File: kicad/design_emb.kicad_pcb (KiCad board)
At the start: 2 copper layers, 79.9 x 98.8 mm, 116 parts, among them J1 Conn_01x04, J2 Barrel_Jack, J3 USB_A, J4 Conn_01x03, J5 Conn_02x11_Counter_Clockwise, J6 Conn_02x10_Counter_Clockwise, J7 Screw_Terminal_01x02, J8 Screw_Terminal_01x02, K1 SANYOU_SRD_Form_C, K2 SANYOU_SRD_Form_C, Q1 MMBT3904, Q2 MMBT3904, SW1 SW_Push, SW3 SW_Push, U1 SRX.X.TCT, U10 S25FL116KOXNFIQ-11, U2 SRX.X.TCT, U3 STM32F446ZETx, U4 ICE40HX1K, U5 TLV1117LV33DCYR, U6 TLV1117LV33DCYR, U7 TLV1117LV12DCYR, U8 OMEGA2, U9 RCLAMP0502B

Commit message: ruteo
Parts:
- moved J3 0.85 mm to (148.8, 94.4)
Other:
- board size 79.9 x 98.8 mm -> 79.8 x 98.9 mm
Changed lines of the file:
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@@
   )
   (module Connectors:USB_A (layer F.Cu)
-    (at 148.844 95.25 180)
+    (at 148.8059 94.3991 180)
     (descr "USB A connector")
     (tags "USB USB_A")
@@
     )
   )
-  (gr_line (start 159.0802 83.0326) (end 79.1718 82.9564) (layer Edge.Cuts) (width 0.15))
-  (gr_line (start 158.9786 181.6989) (end 159.004 83.058) (layer Edge.Cuts) (width 0.15))
-  (gr_line (start 79.2353 181.7878) (end 79.1845 82.9818) (layer Edge.Cuts) (width 0.2))
+  (gr_line (start 158.9913 83.0326) (end 79.1718 82.9564) (layer Edge.Cuts) (width 0.15))
+  (gr_line (start 158.9913 181.7243) (end 159.004 83.058) (layer Edge.Cuts) (width 0.15))
+  (gr_line (start 79.2226 181.7878) (end 79.1718 82.9818) (layer Edge.Cuts) (width 0.2))
   (dimension 99.174366 (width 0.3) (layer F.SilkS)
-    (gr_text "99,174 mm" (at 73.454835 132.075698 89.93396571) (layer F.SilkS)
+    (gr_text "99,174 mm" (at 72.286058 132.546979 89.93396571) (layer F.SilkS)
       (effects (font (size 1.5 1.5) (thickness 0.3)))
     )
-    (feature1 (pts (xy 75.910241 82.491312) (xy 75.025564 82.490292)))
-    (feature2 (pts (xy 75.795941 181.665612) (xy 74.911264 181.664592)))
-    (crossbar (pts (xy 75.497684 181.665268) (xy 75.611984 82.490968)))
-    (arrow1a (pts (xy 75.611984 82.490968) (xy 76.197106 83.618147)))
-    (arrow1b (pts (xy 75.611984 82.490968) (xy 75.024265 83.616795)))
-    (arrow2a (pts (xy 75.497684 181.665268) (xy 76.085403 180.539441)))
-    (arrow2b (pts (xy 75.497684 181.665268) (xy 74.912562 180.538089)))
-  )
-  (gr_line (start 158.9532 181.7243) (end 79.2988 181.8005) (layer Edge.Cuts) (width 0.15))
+    (feature1 (pts (xy 74.741464 82.962593) (xy 73.856787 82.961573)))
+    (feature2 (pts (xy 74.627164 182.136893) (xy 73.742487 182.135873)))
+    (crossbar (pts (xy 74.328907 182.136549) (xy 74.443207 82.962249)))
+    (arrow1a (pts (xy 74.443207 82.962249) (xy 75.028329 84.089428)))
+    (arrow1b (pts (xy 74.443207 82.962249) (xy 73.855488 84.088076)))
+    (arrow2a (pts (xy 74.328907 182.136549) (xy 74.916626 181.010722)))
+    (arrow2b (pts (xy 74.328907 182.136549) (xy 73.743785 181.00937)))
+  )
+  (gr_line (start 158.9913 181.7243) (end 79.2099 181.8132) (layer Edge.Cuts) (width 0.15))
   (dimension 80.086204 (width 0.3) (layer F.SilkS)
     (gr_text "80,086 mm" (at 119.154383 183.078787 0.01817182924) (layer F.SilkS)

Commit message: design_emb.kicad_pcb
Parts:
- C1, D10, R15: moved to B.Cu
- moved Q2 65.6 mm to (94.2, 130.8), turned to 90 degrees
- moved C39 64.0 mm to (120.0, 118.2)
- moved C41 64.0 mm to (120.0, 115.6)
- moved C44 64.0 mm to (120.0, 120.7)
- moved C52 64.0 mm to (120.0, 113.0)
- moved R13 63.0 mm to (90.2, 129.5), turned to 270 degrees
- moved D8 59.9 mm to (94.0, 134.6)
- moved C42 56.0 mm to (125.1, 113.0)
- moved C45 56.0 mm to (125.1, 115.6)
- moved D7 55.0 mm to (99.1, 132.1)
- moved R12 52.4 mm to (99.1, 129.5)
- moved C26 50.9 mm to (125.1, 118.1)
- moved Q1 50.3 mm to (90.2, 125.7), turned to 180 degrees
- moved C43 34.4 mm to (131.4, 88.9)
- moved C40 34.4 mm to (131.4, 91.4)
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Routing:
- net VDD: track 57.8 -> 201.1 mm, vias 2 -> 7
- net Net-(D11-Pad2): track 0.00 -> 75.2 mm, vias 0 -> 2
- net +5VA: track 16.0 -> 82.7 mm, vias 3 -> 4
- net Net-(D12-Pad2): track 0.00 -> 63.2 mm, vias 0 -> 1
- net /SERIAL_TX: track 0.00 -> 58.3 mm, vias 0 -> 1
- net /SERIAL_RX: track 0.00 -> 51.4 mm, vias 0 -> 1
- net GND: track 0.00 -> 40.6 mm, vias 0 -> 1
- net /3V3_O: track 0.00 -> 29.9 mm
- net Net-(J7-Pad2): track 0.00 -> 27.3 mm
- net /Sheet2/RESET: track 0.00 -> 24.7 mm, vias 0 -> 1
- net Net-(J8-Pad1): track 0.00 -> 23.6 mm
- net /Sheet2/USB-: track 0.00 -> 21.4 mm, vias 0 -> 1
- net /Sheet2/SPI1: track 64.4 -> 82.5 mm, vias 1 -> 5
- net /Sheet2/USB+: track 0.00 -> 17.6 mm, vias 0 -> 1
- net Net-(J3-Pad5): track 0.00 -> 16.6 mm
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
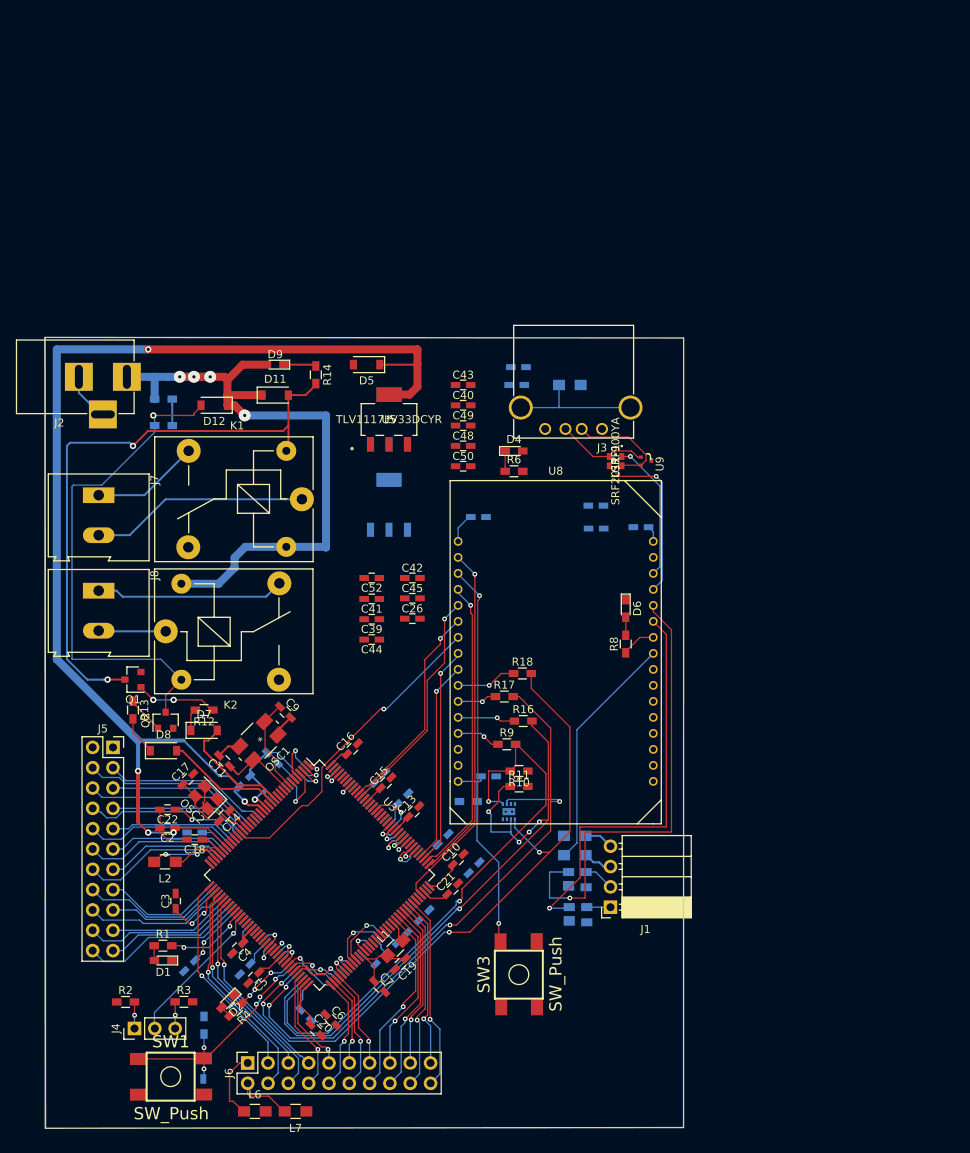
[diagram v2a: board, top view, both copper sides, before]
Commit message: plano de tierra y modificación de señales
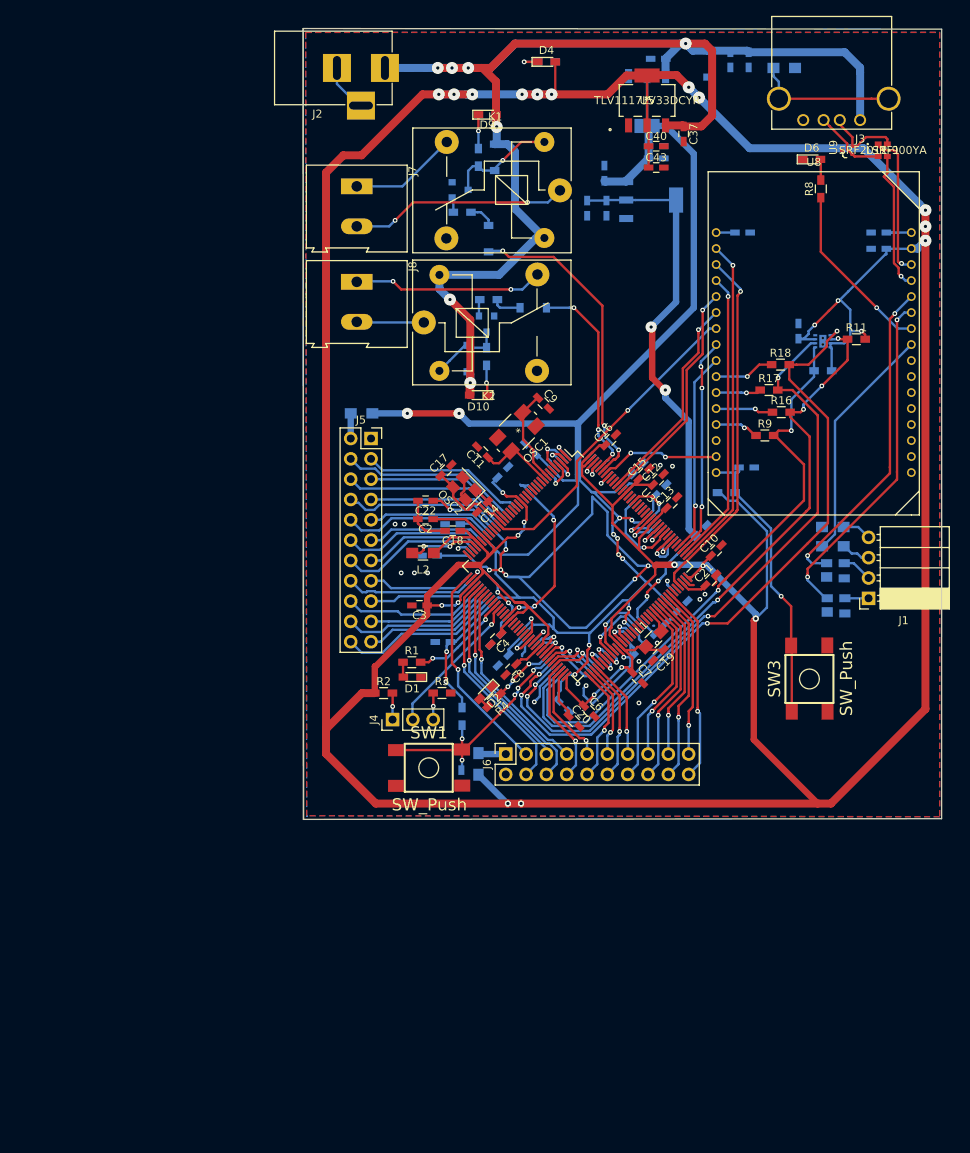
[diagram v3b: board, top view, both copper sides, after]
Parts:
- removed C35, C5: 100nF, Capacitors_SMD:C_0603_HandSoldering
- C12, C37, C8, D10: moved to F.Cu
- C26, C39, C41, C42, C44, C45, C48, C49, C50, C52, D11, D12, D5, D7, D8, L6, L7, Q1, Q2, R10, R12, R13, R14, R6: moved to B.Cu
- moved L7 87.6 mm to (118.7, 92.5), turned to 0 degrees
- moved Q1 73.6 mm to (131.1, 64.5), turned to 0 degrees
- moved D8 72.1 mm to (140.2, 79.2)
- moved D7 71.0 mm to (134.6, 70.6), turned to 270 degrees
- moved U10 70.7 mm to (176.4, 83.4), turned to 90 degrees
- moved R12 70.1 mm to (131.3, 67.3), turned to 0 degrees
- moved R11 70.0 mm to (180.6, 83.2)
- moved C44 69.9 mm to (155.6, 60.6), turned to 0 degrees
- moved R13 67.9 mm to (134.6, 78.2), turned to 0 degrees
- moved C41 66.8 mm to (155.6, 59.1), turned to 0 degrees
- moved Q2 63.7 mm to (134.4, 81.3), turned to 270 degrees
- moved C39 62.9 mm to (149.1, 62.4), turned to 90 degrees
- moved R10 62.8 mm to (176.4, 87.1)
- moved C50 62.1 mm to (167.1, 48.3), turned to 270 degrees
- moved R8 61.9 mm to (176.1, 64.4)
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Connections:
- C1 pad 1: VDD -> /Sheet4/+3V3
- C10 pad 1: VDD -> /Sheet4/+3V3
- C12 pad 1: VDD -> /Sheet4/+3V3
- C13 pad 1: VDD -> /Sheet4/+3V3
- C15 pad 1: VDD -> /Sheet4/+3V3
- C16 pad 1: VDD -> /Sheet4/+3V3
- C18 pad 1: VDD -> /Sheet4/+3V3
- C19 pad 1: VDD -> /Sheet4/+3V3
- C2 pad 1: VDD -> /Sheet4/+3V3
- C3 pad 1: VDD -> /Sheet4/+3V3
- C37 pad 1: /Sheet4/+5V -> +5VA
- C38 pad 1: /Sheet4/+5V -> +5VA
- C4 pad 1: VDD -> /Sheet4/+3V3
- C40 pad 1: VDD -> /Sheet4/+3V3
- C43 pad 1: VDD -> /Sheet4/+3V3
- C48 pad 1: VDD -> /Sheet4/+3V3
- C49 pad 1: VDD -> +5VA
- C50 pad 1: VDD -> +5VA
- C52 pad 1: /Sheet4/+3V3_FPGA -> /Sheet4/+3V3
- C6 pad 1: VDD -> /Sheet4/+3V3
- C7 pad 1: VDD -> /Sheet4/+3V3
- C8 pad 1: VDD -> /Sheet4/+3V3
- D4 pad 2: VDD -> /Sheet4/+3V3
- D5 pad 1: VDD -> +5VA
- J3 pad 1: VDD -> +5VA
- J5 pad 2: /Sheet4/+3V3_FPGA -> Net-(J5-Pad2)
- J6 pad 2: Net-(J6-Pad2) -> GND
- L1 pad 1: VDD -> /Sheet4/+3V3
- L2 pad 1: VDD -> /Sheet4/+3V3
- L6 pad 2: VDD -> /Sheet4/+3V3
- L7 pad 1: GND -> Net-(J5-Pad2)
- L7 pad 2: Net-(J6-Pad2) -> /Sheet4/+3V3_FPGA
- R10 pad 1: /Sheet4/+3V3_FPGA -> /Sheet4/+3V3
- R11 pad 2: /Sheet4/+3V3_FPGA -> /Sheet4/+3V3
- R2 pad 1: VDD -> /Sheet4/+3V3
- R7 pad 1: VDD -> /Sheet4/+3V3
- U10 pad 3: /Sheet4/+3V3_FPGA -> /Sheet4/+3V3
- U10 pad 7: /Sheet4/+3V3_FPGA -> /Sheet4/+3V3
- U10 pad 8: /Sheet4/+3V3_FPGA -> /Sheet4/+3V3
- U3 pad 108: VDD -> /Sheet4/+3V3
- U3 pad 121: VDD -> /Sheet4/+3V3
- U3 pad 13: /Sheet5/IN_REL1 -> Net-(U3-Pad13)
- U3 pad 131: VDD -> /Sheet4/+3V3
- U3 pad 139: Net-(U3-Pad139) -> /Sheet5/IN_REL1
- U3 pad 14: /Sheet5/IN_REL2 -> Net-(U3-Pad14)
- U3 pad 140: Net-(U3-Pad140) -> /Sheet5/IN_REL2
- U3 pad 143: VDD -> /Sheet4/+3V3
- U3 pad 144: VDD -> /Sheet4/+3V3
- U3 pad 17: VDD -> /Sheet4/+3V3
- U3 pad 30: VDD -> /Sheet4/+3V3
- U3 pad 32: VDD -> /Sheet4/+3V3
- U3 pad 39: VDD -> /Sheet4/+3V3
- U3 pad 52: VDD -> /Sheet4/+3V3
- U3 pad 62: VDD -> /Sheet4/+3V3
- U3 pad 72: VDD -> /Sheet4/+3V3
- U3 pad 84: VDD -> /Sheet4/+3V3
- U4 pad 117: /Sheet1/CTRL1 -> Net-(U4-Pad117)
- U4 pad 128: Net-(U4-Pad128) -> /Sheet1/CTRL1
- U5 pad 2: VDD -> /Sheet4/+3V3
- U5 pad 3: /Sheet4/+5V -> +5VA
- U5 pad 4: VDD -> /Sheet4/+3V3
- U6 pad 3: /Sheet4/+5V -> +5VA
- U8 pad 31: VDD -> /Sheet4/+3V3
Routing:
- net /Sheet4/+3V3: track 0.00 -> 622.1 mm, vias 0 -> 26
- net /Sheet4/+3V3_FPGA: track 31.4 -> 238.9 mm, vias 2 -> 14
- net VDD: track 201.1 -> 0.00 mm, vias 7 -> 0
- net /Sheet4/+1V2_FPGA: track 16.0 -> 163.6 mm, vias 1 -> 13
- net +5VA: track 82.7 -> 190.4 mm, vias 4 -> 7
- net Net-(D11-Pad2): track 75.2 -> 14.0 mm, vias 2 -> 1
- net Net-(D12-Pad2): track 63.2 -> 9.30 mm, vias 1 -> 0
- net GND: track 40.6 -> 78.9 mm, vias 1 -> 22
- net /Sheet5/IN_REL1: track 14.8 -> 39.5 mm, vias 0 -> 3
- net /Sheet2/PROBE: track 4.33 -> 22.1 mm, vias 0 -> 1
- net /SERIAL_TX: track 58.3 -> 40.8 mm, vias 1 -> 2
- net /Sheet1/BOOT0: track 0.00 -> 15.1 mm, vias 0 -> 2
- net /Sheet2/RESET: track 24.7 -> 36.3 mm
- net /Sheet5/IN_REL2: track 14.5 -> 26.1 mm, vias 0 -> 3
- net /SERIAL_RX: track 51.4 -> 42.7 mm, vias 1 -> 2
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- added copper zone on B.Cu, net GND
- added copper zone on F.Cu, net GND
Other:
- net class Default: trace_width 0.25 -> 0.3
- net class signals: clearance 0.15 -> 0.154; trace_width 0.25 -> 0.3
- rule trace_min: 0.15 -> 0.3

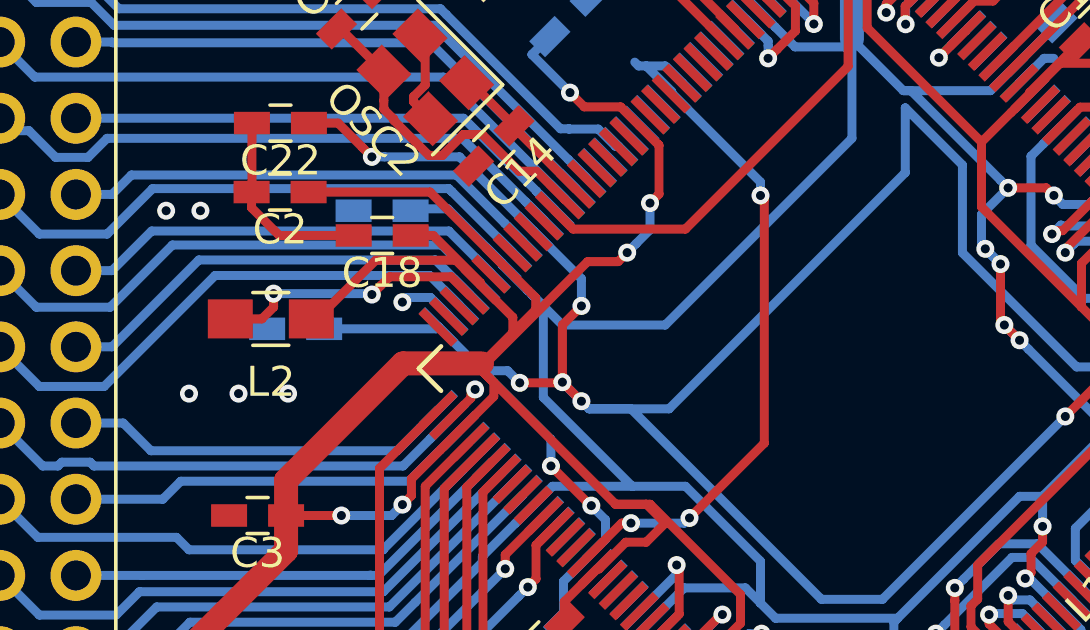
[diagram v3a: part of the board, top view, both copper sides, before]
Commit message: modificación alimentación PLL fpga
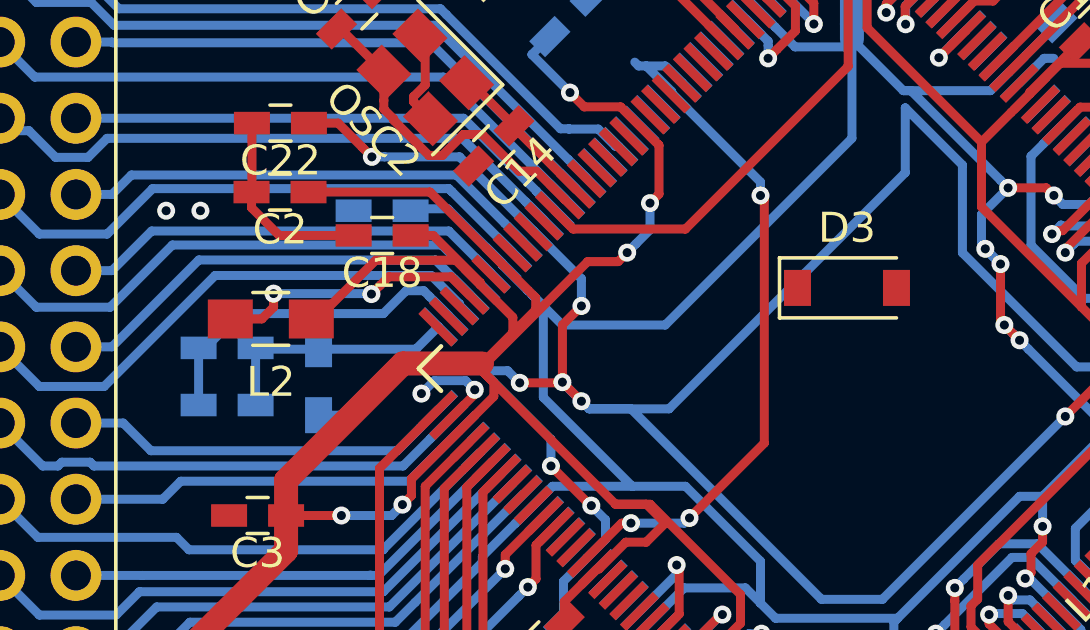
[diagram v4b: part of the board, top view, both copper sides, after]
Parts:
- added C5: 10uF, Capacitors_SMD:C_0603_HandSoldering, B.Cu at (125.0, 112.8)
- added D3: 1N5817, Diodes_SMD:D_SOD-123, F.Cu at (145.6, 108.9)
- added R19: 100, Resistors_SMD:R_0603_HandSoldering, B.Cu at (128.0, 112.0)
- moved C26 2.37 mm to (125.0, 110.9)
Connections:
- C26 pad 1: /Sheet4/+1V2_FPGA -> /sheet3/VCCPLL
- C26 pad 2: GND -> /sheet3/PLLGND
- U4 pad 35: GND -> /sheet3/PLLGND
- U4 pad 36: /Sheet4/+1V2_FPGA -> /sheet3/VCCPLL
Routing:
- net /sheet3/PLLGND: track 0.00 -> 11.4 mm
- net /sheet3/VCCPLL: track 0.00 -> 8.33 mm
- net GND: track 78.9 -> 79.3 mm, vias 22 -> 19

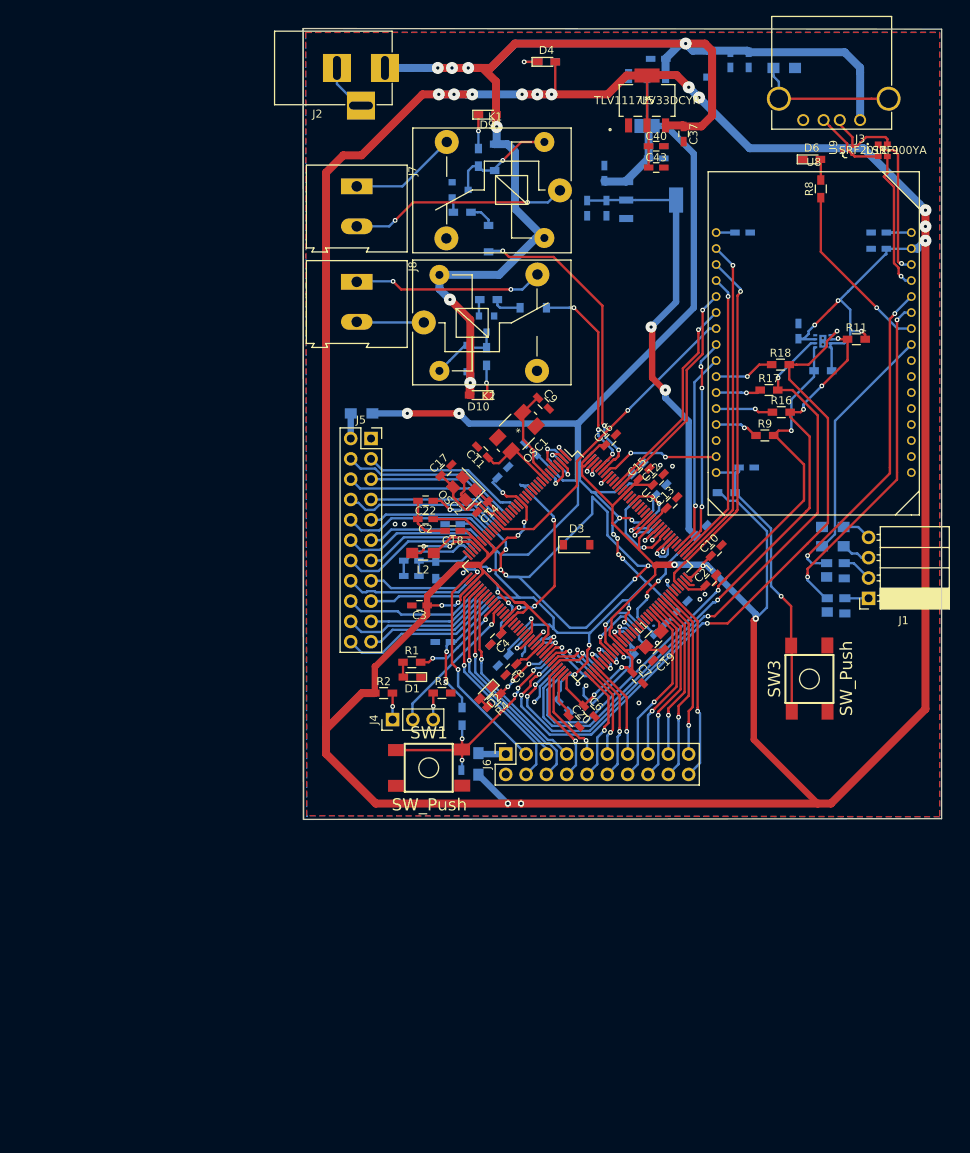
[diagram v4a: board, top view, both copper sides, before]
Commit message: soportes mecánicos y osc fpga
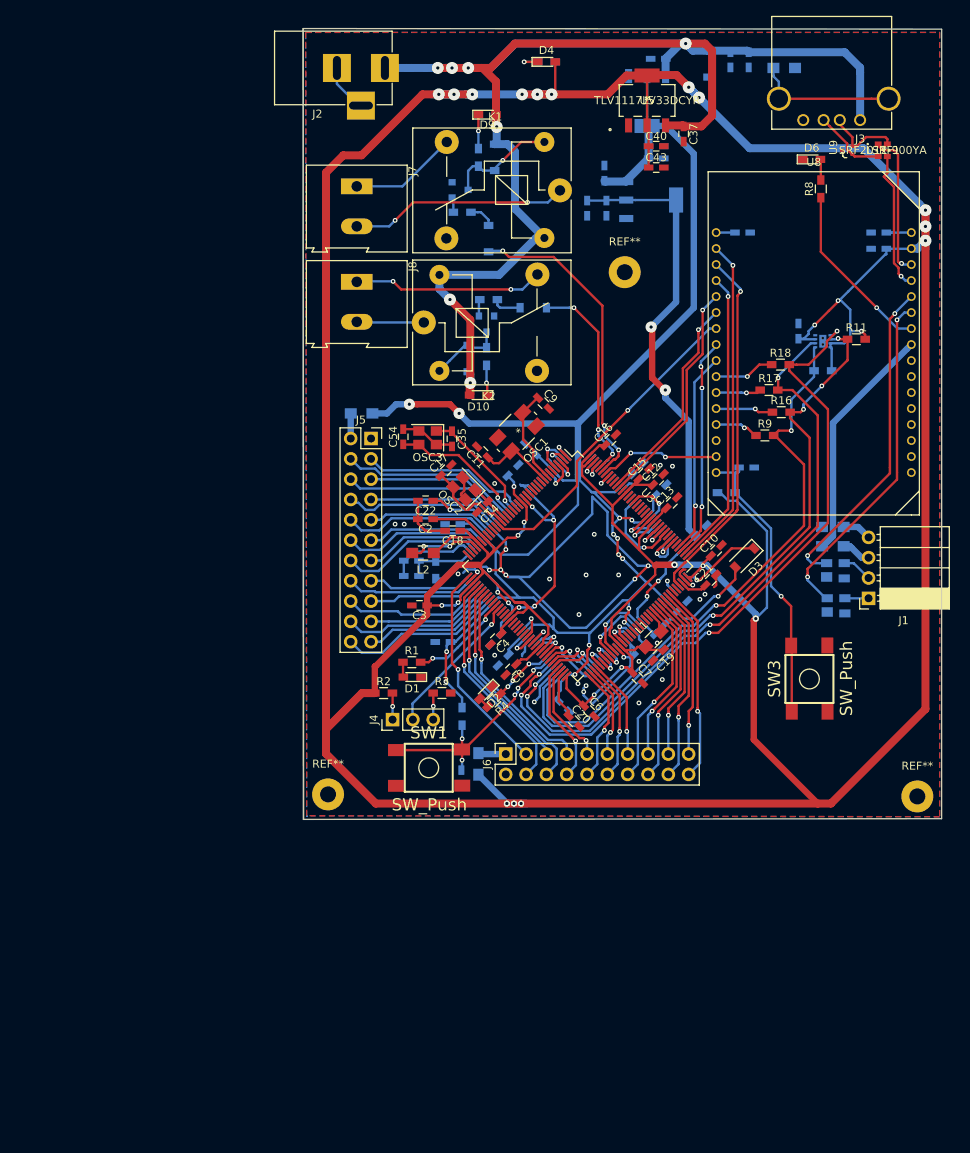
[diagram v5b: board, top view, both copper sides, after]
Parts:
- added C35: 10pF, Capacitors_SMD:C_0603_HandSoldering, F.Cu at (130.0, 95.6)
- added C54: 10pF, Capacitors_SMD:C_0603_HandSoldering, F.Cu at (124.0, 95.4)
- added OSC3: 12MHz, Crystals:Crystal_SMD_Abracon_ABM8G-4pin_3.2x2.5mm, F.Cu at (127.0, 95.5)
- added REF**: SolderWirePad_single_2mmDrill, Wire_Pads:SolderWirePad_single_2mmDrill, F.Cu at (151.6, 74.8)
- added REF**: SolderWirePad_single_2mmDrill, Wire_Pads:SolderWirePad_single_2mmDrill, F.Cu at (188.2, 140.3)
- added REF**: SolderWirePad_single_2mmDrill, Wire_Pads:SolderWirePad_single_2mmDrill, F.Cu at (114.6, 140.1)
- moved D3 21.1 mm to (166.6, 110.5), turned to 225 degrees
- moved C1 1.30 mm to (137.7, 99.6)
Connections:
- U4 pad 20: Net-(U4-Pad20) -> /sheet3/OSC_IN
- U4 pad 21: Net-(U4-Pad21) -> /sheet3/OSC_OUT
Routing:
- net /sheet3/OSC_OUT: track 0.00 -> 17.3 mm, vias 0 -> 1
- net /sheet3/OSC_IN: track 0.00 -> 14.9 mm, vias 0 -> 1
- net GND: track 79.3 -> 93.3 mm, vias 19 -> 30
- net /Sheet4/+3V3: track 622.1 -> 635.7 mm, vias 26 -> 27
- net /Sheet4/+3V3_FPGA: track 238.9 -> 251.1 mm, vias 14 -> 15
- net Net-(D3-Pad1): track 0.00 -> 10.1 mm, vias 0 -> 1
- net /Sheet4/+1V2_FPGA: track 163.9 -> 165.4 mm
- net /Sheet2/SPI1: track 79.8 -> 81.3 mm
- net /Sheet2/SPI0: track 74.6 -> 75.7 mm
- net /Sheet2/SPI2: track 82.1 -> 83.1 mm
- net /Sheet1/USR5: track 25.1 -> 25.8 mm
